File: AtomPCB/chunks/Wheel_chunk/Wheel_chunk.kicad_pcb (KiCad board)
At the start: 2 copper layers, 37 x 49 mm, 31 parts, among them J1 DF40HC_4.0_-40DS-0.4V_70_, J2 Conn_01x04_Pin, J3 Conn_01x04_Pin, J4 Conn_01x04_Pin, J5 Conn_01x04_Pin, U1 ATtiny416-M, U3 DRV8834RGER, U4 DRV8834RGER, U6 MPM3610AGQV-P

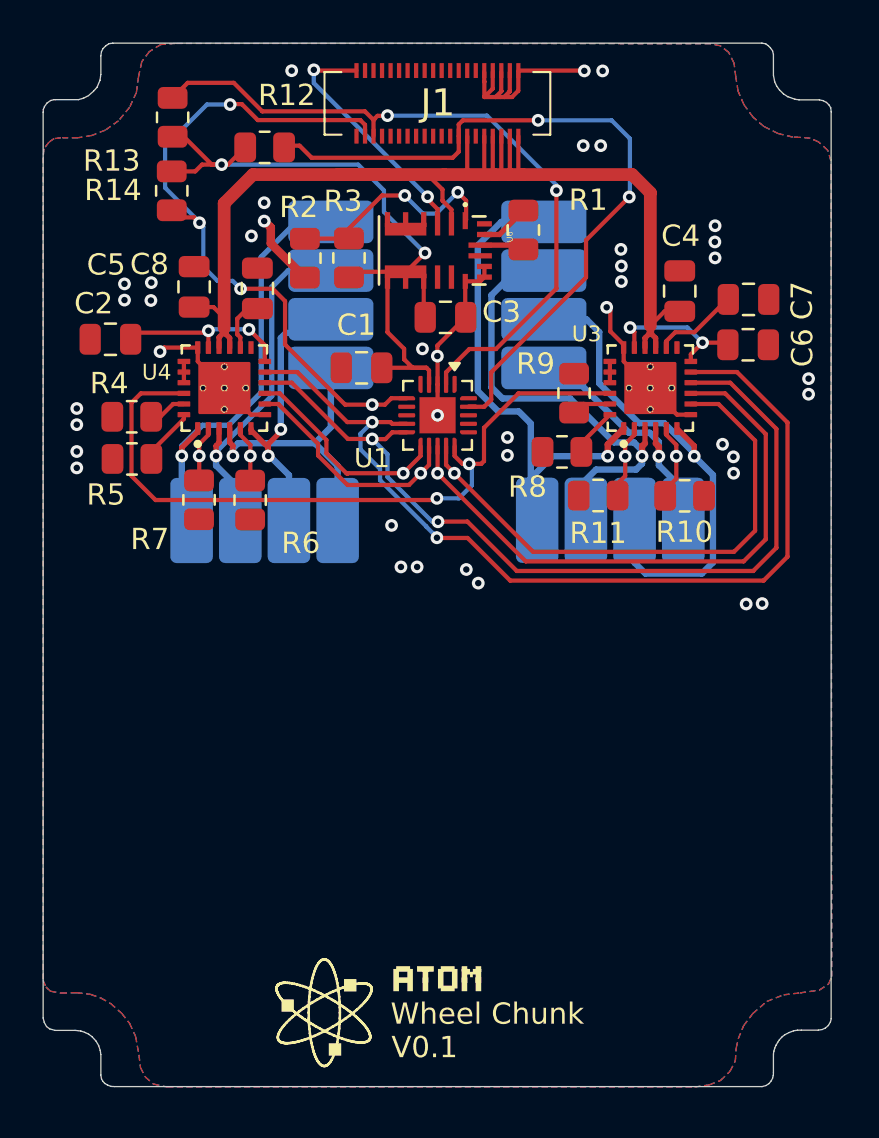
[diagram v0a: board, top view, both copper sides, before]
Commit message: adding wheel chunk updates, fixing buck wiring issues
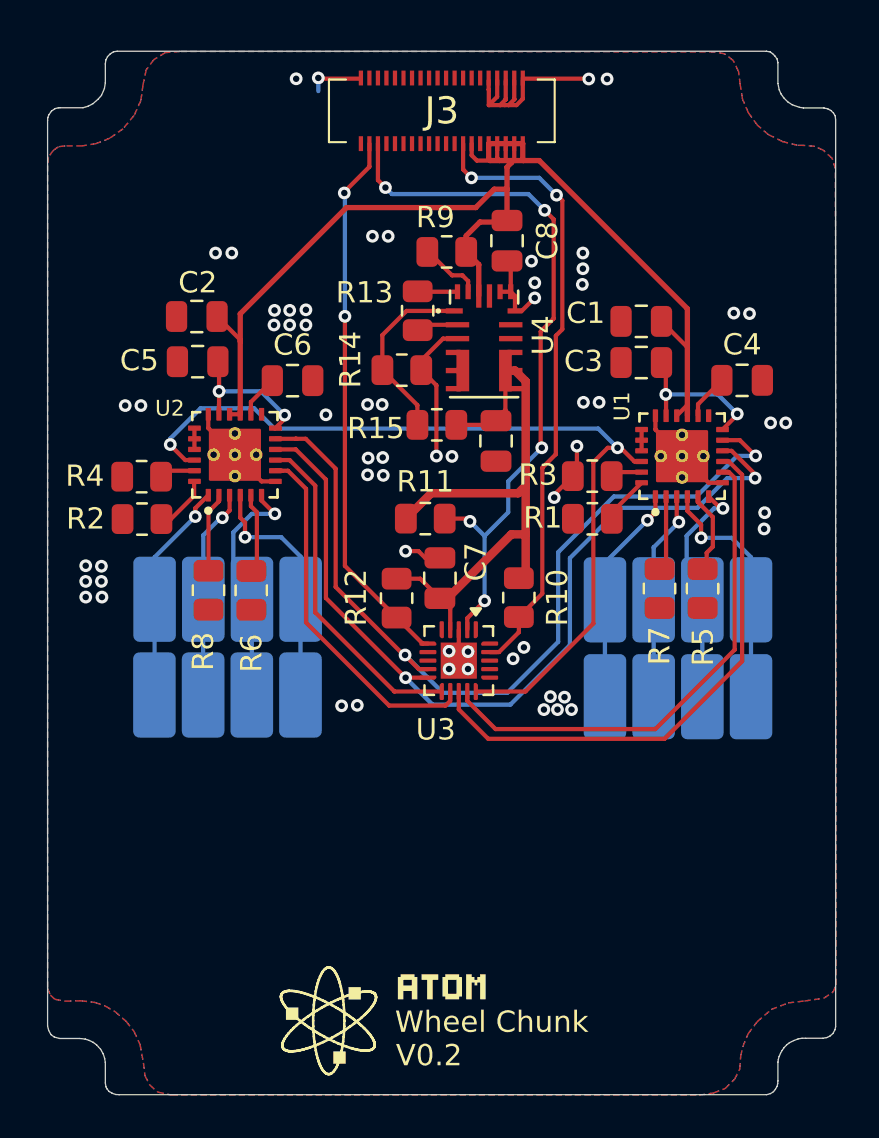
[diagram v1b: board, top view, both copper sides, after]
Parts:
- removed U6: MPM3610AGQV-P, MPM3610AGQV-P:CONV_MPM3620AGQV-P
- added C9: 22uF, Capacitor_SMD:C_0805_2012Metric, F.Cu at (129.8, 117.5)
- added R15: 75K, Resistor_SMD:R_0805_2012Metric, F.Cu at (127.0, 116.7)
- added U2: DRV8834RGER, DRV8834:DRIVER_DRV8834RGER, F.Cu at (117.5, 118.1)
- C1: value 22uF -> 10uf
- C2: value 2.2uf -> 10uf
- C3: value 22uF -> 2.2uf
- C4: value 10uf -> 0.01uf
- C5: value 10uf -> 2.2uf
- C6: value 2.2uf -> 0.01uf
- C7: value 0.01uf -> 22uF
- C8: value 0.01uf -> 10uF
- J1: value DF40HC_4.0_-40DS-0.4V_70_ -> Conn_01x04_Pin; footprint HIROSE_DF40HC_40_connector:DF40HC4040DS04V70 -> Wire_flat_pads:PAD_1x4_4.0x2.0; moved to B.Cu
- J3: value Conn_01x04_Pin -> DF40HC_4.0_-40DS-0.4V_70_; footprint Wire_flat_pads:PAD_1x4_4.0x2.0 -> HIROSE_DF40HC_40_connector:DF40HC4040DS04V70; moved to F.Cu
- R1, R3: value 75K -> 50k
- R10: value 50k -> 10K
- R11: value 50k -> 4.7K
- R12: value 10K -> 4.7K
- R13: value 4.7K -> 100k
- R14: value 4.7K -> 24K
- R2: value 24K -> 50k
- R9: value 50k -> 75K
- U1: value ATtiny416-M -> DRV8834RGER; footprint Package_DFN_QFN:VQFN-20-1EP_3x3mm_P0.4mm_EP1.7x1.7mm -> DRV8834:DRIVER_DRV8834RGER
- U3: value DRV8834RGER -> ATtiny416-M; footprint DRV8834:DRIVER_DRV8834RGER -> Package_DFN_QFN:VQFN-20-1EP_3x3mm_P0.4mm_EP1.7x1.7mm
- U4: value DRV8834RGER -> MPM3610AGQV-P; footprint DRV8834:DRIVER_DRV8834RGER -> MPM3610AGQV-P:CONV_MPM3620AGQV-P
- moved J1 28.9 mm to (134.9, 129.5), turned to -90 degrees
- moved R5 27.5 mm to (139.5, 124.4), turned to -90 degrees
- moved R12 22.1 mm to (125.1, 124.9), turned to 90 degrees
- moved R7 22.0 mm to (137.4, 124.4)
- moved C6 21.5 mm to (120.2, 114.7)
- moved J3 19.7 mm to (127.2, 102.0), turned to 0 degrees
- moved J4 19.6 mm to (113.7, 124.9), turned to -90 degrees
- moved C7 19.5 mm to (127.1, 123.9), turned to -90 degrees
- moved J2 18.0 mm to (134.9, 124.9), turned to -90 degrees
- moved R8 17.8 mm to (116.3, 124.5), turned to -90 degrees
- moved U3 15.6 mm to (128.0, 127.8), turned to -90 degrees
- moved R3 15.3 mm to (134.3, 119.1), turned to 180 degrees
- moved R13 14.7 mm to (126.1, 111.4), turned to 90 degrees
- moved R2 14.4 mm to (113.1, 121.2), turned to 180 degrees
- moved R1 13.9 mm to (134.3, 121.1), turned to 180 degrees
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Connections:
- C1 pad 1: GND -> VBATT
- C1 pad 2: 3.3V -> GND
- C2 pad 1: /CFG2 -> VBATT
- C3 pad 1: 3.3V -> /CFG1
- C4 pad 1: VBATT -> Net-(U1-VCP)
- C5 pad 1: VBATT -> /CFG2
- C6 pad 1: /CFG1 -> Net-(U2-VCP)
- C7 pad 1: Net-(U3-VCP) -> GND
- C7 pad 2: GND -> 3.3V
- C8 pad 1: Net-(U4-VCP) -> GND
- C8 pad 2: GND -> VBATT
- J1 pad 1: unconnected-(J1-Pad1) -> /M1A+
- J1 pad 2: GND -> /M1A-
- J1 pad 3: /SCL1 -> /M1B+
- J1 pad 4: /SDA2 -> /M1B-
- J3 pad 1: /M1A+ -> unconnected-(J3-Pad1)
- J3 pad 2: /M1A- -> GND
- J3 pad 3: /M1B+ -> /SCL1
- J3 pad 4: /M1B- -> /SDA2
- R1 pad 1: VIN -> Net-(U1-ADECAY)
- R1 pad 2: Net-(U6-EN) -> GND
- R10 pad 1: Net-(U3-BISEN) -> /UPDI
- R10 pad 2: GND -> 3.3V
- R11 pad 1: Net-(U3-AISEN) -> /SDA1
- R11 pad 2: GND -> 3.3V
- R12 pad 1: /UPDI -> /SCL1
- R13 pad 1: /SDA1 -> 4.9V
- R13 pad 2: 3.3V -> Net-(U4-PG)
- R14 pad 1: /SCL1 -> GND
- R14 pad 2: 3.3V -> Net-(U4-FB)
- R2 pad 1: GND -> Net-(U2-ADECAY)
- R2 pad 2: Net-(U6-FB) -> GND
- R3 pad 1: 3.3V -> Net-(U1-BDECAY)
- R3 pad 2: Net-(U6-FB) -> GND
- R4 pad 1: Net-(U4-BDECAY) -> Net-(U2-BDECAY)
- R5 pad 1: Net-(U4-ADECAY) -> Net-(U1-BISEN)
- R6 pad 1: Net-(U4-BISEN) -> Net-(U2-BISEN)
- R7 pad 1: Net-(U4-AISEN) -> Net-(U1-AISEN)
- R8 pad 1: Net-(U3-ADECAY) -> Net-(U2-AISEN)
- R9 pad 1: Net-(U3-BDECAY) -> VBATT
- R9 pad 2: GND -> Net-(U4-EN)
- U1 pad 1: unconnected-(U1-PA2-Pad1) -> /M1A+
- U1 pad 11: /DIR_2 -> /MICRO_STEP_SEL_2
- U1 pad 12: /STEP_2 -> /CFG1
- U1 pad 13: /DIR_1 -> unconnected-(U1-NFAULT-Pad13)
- U1 pad 14: /STEP_1 -> Net-(U1-VCP)
- U1 pad 15: /EN -> VBATT
- U1 pad 16: unconnected-(U1-PC1-Pad16) -> VBATT
- U1 pad 17: unconnected-(U1-PC2-Pad17) -> /CFG1
- U1 pad 18: unconnected-(U1-PC3-Pad18) -> GND
- U1 pad 19: /UPDI -> /REF1
- U1 pad 2: /SDA1 -> Net-(U1-AISEN)
- U1 pad 20: unconnected-(U1-PA1-Pad20) -> /REF1
- U1 pad 21: GND -> /REF1
- U1 pad 3: GND -> /M1A-
- U1 pad 4: 3.3V -> /M1B-
- U1 pad 5: unconnected-(U1-PA4-Pad5) -> Net-(U1-BISEN)
- U1 pad 6: /SCL1 -> /M1B+
- U1 pad 7: unconnected-(U1-PA6-Pad7) -> GND
- U1 pad 8: unconnected-(U1-PA7-Pad8) -> /STEP_1
- U1 pad 9: /MICRO_STEP_SEL_2 -> /DIR_1
- U3 pad 1: /M1A+ -> unconnected-(U3-PA2-Pad1)
- U3 pad 11: /MICRO_STEP_SEL_2 -> /DIR_2
- U3 pad 12: /CFG1 -> /STEP_2
- U3 pad 13: unconnected-(U3-NFAULT-Pad13) -> /DIR_1
- U3 pad 14: Net-(U3-VCP) -> /STEP_1
- U3 pad 15: VBATT -> /EN
- U3 pad 16: VBATT -> unconnected-(U3-PC1-Pad16)
- U3 pad 17: /CFG1 -> unconnected-(U3-PC2-Pad17)
- U3 pad 18: GND -> unconnected-(U3-PC3-Pad18)
- U3 pad 19: /REF1 -> /UPDI
- U3 pad 2: Net-(U3-AISEN) -> /SDA1
- U3 pad 20: /REF1 -> unconnected-(U3-PA1-Pad20)
- U3 pad 21: /REF1 -> GND
- U3 pad 3: /M1A- -> GND
- U3 pad 4: /M1B- -> 3.3V
- U3 pad 5: Net-(U3-BISEN) -> unconnected-(U3-PA4-Pad5)
- U3 pad 6: /M1B+ -> /SCL1
- U3 pad 7: GND -> unconnected-(U3-PA6-Pad7)
- U3 pad 8: /STEP_1 -> unconnected-(U3-PA7-Pad8)
- U3 pad 9: /DIR_1 -> /MICRO_STEP_SEL_2
- U4 pad 1: /M3A+ -> Net-(U4-FB)
- U4 pad 10: /MICRO_STEP_SEL_1 -> (no net)
- U4 pad 11: /MICRO_STEP_SEL_2 -> unconnected-(U4-BST-Pad11)
- U4 pad 12: /CFG2 -> GND
- U4 pad 13: unconnected-(U4-NFAULT-Pad13) -> GND
- U4 pad 14: Net-(U4-VCP) -> GND
- U4 pad 15: VBATT -> (no net)
- U4 pad 17: /CFG2 -> Net-(U4-EN)
- U4 pad 18: GND -> Net-(U4-PG)
- U4 pad 2: Net-(U4-AISEN) -> 4.9V
- U4 pad 3: /M3A- -> GND
- U4 pad 4: /M3B- -> Net-(U4-SW-Pad19)
- U4 pad 7: GND -> 3.3V
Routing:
- net /M1A+: track 25.9 -> 10.4 mm
- net /M1B+: track 24.6 -> 11.0 mm
- net /M1A-: track 22.6 -> 9.93 mm
- net Net-(U6-FB): track 10.6 -> 0.00 mm, vias 2 -> 0
- net /M3A+: track 20.9 -> 10.4 mm
- net Net-(U4-FB): track 0.00 -> 8.74 mm
- net GND: track 47.9 -> 40.2 mm, vias 43 -> 61
- net /M3A-: track 17.5 -> 9.94 mm
- net /EN: track 34.1 -> 41.3 mm
- net /SCL1: track 32.6 -> 25.7 mm, vias 4 -> 2
- net /STEP_2: track 10.9 -> 17.3 mm, vias 1 -> 0
- net /DIR_2: track 10.0 -> 15.8 mm, vias 1 -> 0
- net /UPDI: track 34.8 -> 29.4 mm
- net Net-(U3-VCP): track 4.02 -> 0.00 mm
- net Net-(U1-BISEN): track 0.00 -> 3.89 mm
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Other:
- outline, holes or cut-outs redrawn
- board text added: "V0.2"
- board text removed: "M1"
- board text removed: "M2"
- board text removed: "M3"
- board text removed: "M4"
- board text removed: "V0.1"
